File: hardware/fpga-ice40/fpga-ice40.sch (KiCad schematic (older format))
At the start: 88 parts, among them J1 MicroSD_Molex_1040310811, J2 Conn_01x03, J4 Conn_02x20_Odd_Even, J5 USB_B_Micro, J6 Conn_02x05_Odd_Even, J7 Conn_02x05_Odd_Even, Q1 2N7002H, U1 iCE40HX4K-TQ144, U2 IS42S16320F-6TL, U3 W25Q32JVSS, U4 W25Q32JVSS, U5 S25FL256SAGMFI01, U6 S25FL256SAGMFI01, U7 FT245RL, U8 AZ1117-1.2, U9 AZ1117-1.2, X1 ECS-2520MV-xxx-xx

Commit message: Clean up overhanging silkscreen on main 2x20 header
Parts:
- J4: footprint Connector_PinHeader_2.54mm:PinHeader_2x20_P2.54mm_Horizontal -> local_conn:PinHeader_2x20_P2.54mm_Horizontal
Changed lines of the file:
@@
 F 0 "J4" H 8950 15150 50  0000 C CNN
 F 1 "Conn_02x20_Odd_Even" H 8950 15125 50  0001 C CNN
-F 2 "Connector_PinHeader_2.54mm:PinHeader_2x20_P2.54mm_Horizontal" H 8900 14100 50  0001 C CNN
+F 2 "local_conn:PinHeader_2x20_P2.54mm_Horizontal" H 8900 14100 50  0001 C CNN
 F 3 "~" H 8900 14100 50  0001 C CNN
 	1    8900 14100

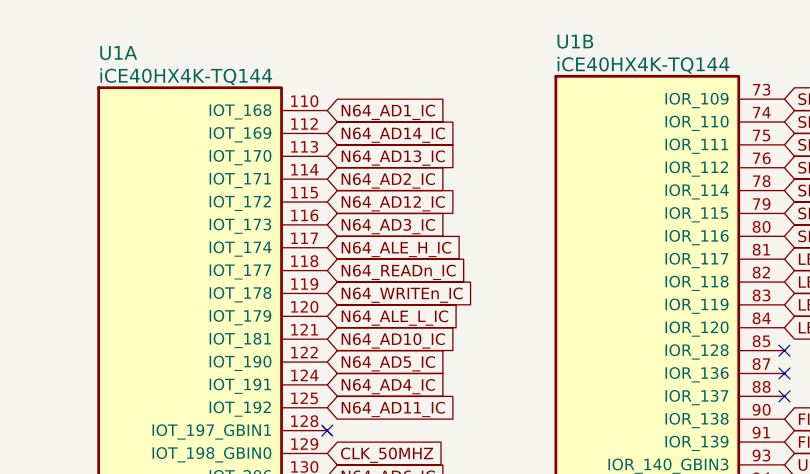
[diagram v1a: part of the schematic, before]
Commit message: N64 cart bus track glossing and front silkscreen cleanup
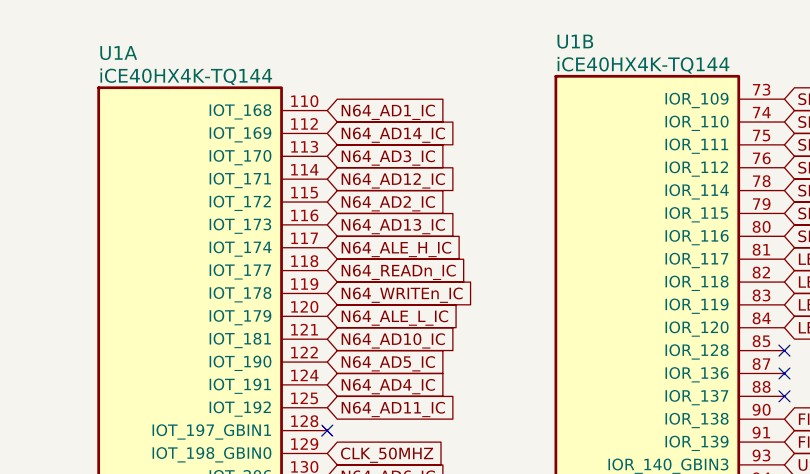
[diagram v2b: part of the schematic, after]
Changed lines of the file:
@@
 Text GLabel 2500 1600 2    50   Input ~ 0
 N64_AD1_IC
-Text GLabel 2500 1900 2    50   Input ~ 0
+Text GLabel 2500 2000 2    50   Input ~ 0
 N64_AD2_IC
-Text GLabel 2500 2100 2    50   Input ~ 0
+Text GLabel 2500 1800 2    50   Input ~ 0
 N64_AD3_IC
 Text GLabel 2500 2500 2    50   Input ~ 0
@@
 Text GLabel 2500 2300 2    50   Input ~ 0
 N64_READn_IC
-Text GLabel 2500 1800 2    50   Input ~ 0
+Text GLabel 2500 2100 2    50   Input ~ 0
 N64_AD13_IC
-Text GLabel 2500 2000 2    50   Input ~ 0
+Text GLabel 2500 1900 2    50   Input ~ 0
 N64_AD12_IC
 Text GLabel 2500 2900 2    50   Input ~ 0

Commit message: Use FTSH footprint with mating geometry and cleanup silkscreen
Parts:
- J6, J7: footprint ng_conn:Samtec_FTSH-105-XX-X-DV -> ng_conn:Samtec_FTSH-105-XX-X-DV-Mating
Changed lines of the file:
@@
 F 0 "J6" H 21700 7250 50  0000 C CNN
 F 1 "Conn_02x05_Odd_Even" H 21700 7276 50  0001 C CNN
-F 2 "ng_conn:Samtec_FTSH-105-XX-X-DV" H 21650 6950 50  0001 C CNN
+F 2 "ng_conn:Samtec_FTSH-105-XX-X-DV-Mating" H 21650 6950 50  0001 C CNN
 F 3 "~" H 21650 6950 50  0001 C CNN
 	1    21650 6950
@@
 F 0 "J7" H 21650 9350 50  0000 C CNN
 F 1 "Conn_02x05_Odd_Even" H 21650 9376 50  0001 C CNN
-F 2 "ng_conn:Samtec_FTSH-105-XX-X-DV" H 21600 9050 50  0001 C CNN
+F 2 "ng_conn:Samtec_FTSH-105-XX-X-DV-Mating" H 21600 9050 50  0001 C CNN
 F 3 "~" H 21600 9050 50  0001 C CNN
 	1    21600 9050

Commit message: Cleanup routing
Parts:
- X1: footprint Oscillator:Oscillator_SMD_ECS_2520MV-xxx-xx-4Pin_2.5x2.0mm -> ng_time:Oscillator_2.5x2.0
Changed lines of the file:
@@
 Text GLabel 21300 9150 0    50   Input ~ 0
 FLASH_MISO|IO1
-Text GLabel 21300 9250 0    50   Input ~ 0
-FLASH_IO2
-Text GLabel 21300 8950 0    50   Input ~ 0
-FLASH_IO3
 Wire Wire Line
 	12350 2450 12450 2450
@@
 Text GLabel 12950 13500 0    50   Input ~ 0
 N64_AD10
-Text GLabel 12950 14100 0    50   Input ~ 0
+Text GLabel 12950 14000 0    50   Input ~ 0
 N64_AD9
-Text GLabel 12950 14300 0    50   Input ~ 0
+Text GLabel 12950 14200 0    50   Input ~ 0
 N64_AD8
 $Comp
@@
 Text GLabel 12950 13600 0    50   Input ~ 0
 N64_AD5
-Text GLabel 12950 14000 0    50   Input ~ 0
+Text GLabel 12950 14100 0    50   Input ~ 0
 N64_AD6
-Text GLabel 12950 14200 0    50   Input ~ 0
+Text GLabel 12950 14300 0    50   Input ~ 0
 N64_AD7
 Text GLabel 11500 13400 2    50   Input ~ 0
@@
 Text GLabel 13350 13500 2    50   Input ~ 0
 N64_AD10_IC
-Text GLabel 13350 14100 2    50   Input ~ 0
+Text GLabel 13350 14000 2    50   Input ~ 0
 N64_AD9_IC
-Text GLabel 13350 14300 2    50   Input ~ 0
+Text GLabel 13350 14200 2    50   Input ~ 0
 N64_AD8_IC
 Text GLabel 13350 14800 2    50   Input ~ 0
@@
 Text GLabel 13350 13600 2    50   Input ~ 0
 N64_AD5_IC
-Text GLabel 13350 14000 2    50   Input ~ 0
+Text GLabel 13350 14100 2    50   Input ~ 0
 N64_AD6_IC
-Text GLabel 13350 14200 2    50   Input ~ 0
+Text GLabel 13350 14300 2    50   Input ~ 0
 N64_AD7_IC
 Text GLabel 4500 4350 2    50   Input ~ 0
@@
 Text GLabel 2500 2400 2    50   Input ~ 0
 N64_WRITEn_IC
+Text GLabel 2500 2100 2    50   Input ~ 0
+N64_READn_IC
 Text GLabel 2500 2300 2    50   Input ~ 0
-N64_READn_IC
-Text GLabel 2500 2100 2    50   Input ~ 0
 N64_AD13_IC
 Text GLabel 2500 1900 2    50   Input ~ 0
@@
 Text GLabel 2500 2600 2    50   Input ~ 0
 N64_AD10_IC
-Text GLabel 2500 3300 2    50   Input ~ 0
+Text GLabel 2500 3200 2    50   Input ~ 0
 N64_AD9_IC
-Text GLabel 2500 3500 2    50   Input ~ 0
+Text GLabel 2500 3400 2    50   Input ~ 0
 N64_AD8_IC
 Text GLabel 2500 3700 2    50   Input ~ 0
@@
 Text GLabel 2500 2700 2    50   Input ~ 0
 N64_AD5_IC
-Text GLabel 2500 3200 2    50   Input ~ 0
+Text GLabel 2500 3300 2    50   Input ~ 0
 N64_AD6_IC
-Text GLabel 2500 3400 2    50   Input ~ 0
+Text GLabel 2500 3500 2    50   Input ~ 0
 N64_AD7_IC
 Text GLabel 8500 2800 2    50   Input ~ 0
@@
 NoConn ~ 21900 9150
 Wire Wire Line
-	21300 8950 21400 8950
-Wire Wire Line
 	21400 9250 21300 9250
 Wire Wire Line
@@
 F 0 "X1" H 14900 3250 50  0000 L CNN
 F 1 "ECS-2520MV-xxx-xx" H 14850 2750 50  0000 L CNN
-F 2 "Oscillator:Oscillator_SMD_ECS_2520MV-xxx-xx-4Pin_2.5x2.0mm" H 15250 2650 50  0001 C CNN
+F 2 "ng_time:Oscillator_2.5x2.0" H 15250 2650 50  0001 C CNN
 F 3 "https://www.ecsxtal.com/store/pdf/ECS-2520MV.pdf" H 14625 3125 50  0001 C CNN
 	1    14800 3000
@@
 	1    0    0    -1
 $EndComp
+Text GLabel 21300 9250 0    50   Input ~ 0
+FLASH_IO2
+Wire Wire Line
+	21300 8950 21400 8950
+Text GLabel 21300 8950 0    50   Input ~ 0
+FLASH_IO3
 $EndSCHEMATC

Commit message: Divide 'fpga-ice40' schematic into multiple sheets
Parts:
- removed C1, C10, C11, C12, C13, C14, C15, C16, C17, C18, C19, C2, C20, C21, C22, C23, C24, C26, C28, C29, C3, C33, C4, C41, C43, C6, C7, C8, C9: 100n, Capacitor_SMD:C_0603_1608Metric, symbol Device:C
- removed C25, C30, C31, C5: 10u, Capacitor_SMD:C_0603_1608Metric, symbol Device:C
- removed C27, C34, C35, C36, C37, C38, C44: 10u, Capacitor_SMD:C_0805_2012Metric, symbol Device:C
- removed C32: 1u, Capacitor_SMD:C_0603_1608Metric, symbol Device:C
- removed C39, C40, C42: 10n, Capacitor_SMD:C_0603_1608Metric, symbol Device:C
- removed D1: ~~800mVf, Diode_SMD:D_SOD-123, symbol Device:D_Schottky
- removed D2, D3, D4, D5, D6: Blue, LED_SMD:LED_0603_1608Metric, symbol Device:LED
- removed FB1: 33R, 500mA, Inductor_SMD:L_0603_1608Metric, symbol Device:Ferrite_Bead
- removed J1: MicroSD_Molex_1040310811, ng_conn:MicroSD_Molex_1040310811, symbol ng_conn:MicroSD_Molex_1040310811
- removed J2: Conn_01x03, Connector_PinHeader_2.54mm:PinHeader_1x03_P2.54mm_Vertical, symbol Connector_Generic:Conn_01x03
- removed J4: Conn_02x20_Odd_Even, local_conn:PinHeader_2x20_P2.54mm_Horizontal, symbol Connector_Generic:Conn_02x20_Odd_Even
- removed J5: USB_B_Micro, Connector_USB:USB_Micro-B_Molex_47346-0001, symbol ng_conn:USB_B_Micro
- removed J6, J7: Conn_02x05_Odd_Even, ng_conn:Samtec_FTSH-105-XX-X-DV-Mating, symbol Connector_Generic:Conn_02x05_Odd_Even
- removed Q1: 2N7002H, Package_TO_SOT_SMD:SOT-23, symbol Transistor_FET:2N7002H
- removed R1, R2, R4, R8, R9: 10k, Resistor_SMD:R_0603_1608Metric, symbol Device:R
- removed R11, R12: 100R, Resistor_SMD:R_0603_1608Metric, symbol Device:R
- removed R3: 6k8, Resistor_SMD:R_0603_1608Metric, symbol Device:R
- removed R5: 470R, Resistor_SMD:R_0603_1608Metric, symbol Device:R
- removed R6: 100k, Resistor_SMD:R_0603_1608Metric, symbol Device:R
- removed R7: 330R, Resistor_SMD:R_Array_Convex_4x0603, symbol Device:R_Pack04_Split
- removed RN1, RN2, RN3: 10k, Resistor_SMD:R_Array_Convex_4x0603, symbol Device:R_Pack04
- removed RN4, RN5, RN6, RN7, RN8, RN9: 33R, Resistor_SMD:R_Array_Convex_4x0603, symbol Device:R_Pack04
- removed U1: iCE40HX4K-TQ144, Package_QFP:TQFP-144_20x20mm_P0.5mm, symbol ng_fpga_lattice_ice40:iCE40HX4K-TQ144
- removed U2: IS42S16320F-6TL, Package_SO:TSOP-II-54_22.2x10.16mm_P0.8mm, symbol ng_memory:IS42S16320F-6TL
- removed U3, U4: W25Q32JVSS, local_hacks:SOIC-8_5.275x5.275mm_P1.27mm__No_CrtYd, symbol ng_memory:W25Q32JVSS
- removed U5, U6: S25FL256SAGMFI01, Package_SO:SOIC-16W_7.5x10.3mm_P1.27mm, symbol ng_memory:S25FL256SAGMFI01
- removed U7: FT245RL, Package_SO:SSOP-28_5.3x10.2mm_P0.65mm, symbol ng_ftdi:FT245RL
- removed U8, U9: AZ1117-1.2, Package_TO_SOT_SMD:SOT-223-3_TabPin2, symbol Regulator_Linear:AZ1117-1.2
- removed X1: ECS-2520MV-xxx-xx, ng_time:Oscillator_2.5x2.0, symbol Oscillator:ECS-2520MV-xxx-xx
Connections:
- net labels removed: CLK_50MHZ, CONFIG_IO2, CONFIG_IO3, CONFIG_MISO|IO1, CONFIG_MOSI|IO0, CONFIG_SCK, CONFIG_SSn, DRAM_A0, DRAM_A1, DRAM_A10, DRAM_A11, DRAM_A12, DRAM_A2, DRAM_A3, DRAM_A4, DRAM_A5, DRAM_A6, DRAM_A7, DRAM_A8, DRAM_A9, DRAM_BA0, DRAM_BA1, DRAM_CASn, DRAM_CKE, DRAM_CLK, DRAM_CSn, DRAM_DQ0, DRAM_DQ1, DRAM_DQ10, DRAM_DQ11, DRAM_DQ12, DRAM_DQ13, DRAM_DQ14, DRAM_DQ15, DRAM_DQ2, DRAM_DQ3, DRAM_DQ4, DRAM_DQ5, DRAM_DQ6, DRAM_DQ7, DRAM_DQ8, DRAM_DQ9, DRAM_LDQM, DRAM_RASn, DRAM_UDQM, DRAM_WEn, FIFO_D0, FIFO_D1, FIFO_D2, FIFO_D3, FIFO_D4, FIFO_D5, FIFO_D6, FIFO_D7, FIFO_RDn, FIFO_RXFn, FIFO_TXEn, FIFO_WR, FLASH_IO2, FLASH_IO3, FLASH_MISO|IO1, FLASH_MOSI|IO0, FLASH_SCK, FLASH_SSn, FPGA_CDONE, FPGA_CRESETn, GND, LED_D0, LED_D1, LED_D2, LED_D3, N64_3V3, N64_AD0, N64_AD0_IC, N64_AD1, N64_AD10, N64_AD10_IC, N64_AD11, N64_AD11_IC, N64_AD12, N64_AD12_IC, N64_AD13, N64_AD13_IC, N64_AD14, N64_AD14_IC, N64_AD15, N64_AD15_IC, N64_AD1_IC, N64_AD2, N64_AD2_IC, N64_AD3, N64_AD3_IC, N64_AD4, N64_AD4_IC, N64_AD5, N64_AD5_IC, N64_AD6, N64_AD6_IC, N64_AD7, N64_AD7_IC, N64_AD8, N64_AD8_IC, N64_AD9, N64_AD9_IC, N64_ALE_H, N64_ALE_H_IC, N64_ALE_L, N64_ALE_L_IC, N64_COLD_RESETn, N64_COLD_RESETn_IC, N64_OS_EVENTn, N64_OS_EVENTn_IC, N64_READn, N64_READn_IC, N64_WRITEn, N64_WRITEn_IC, P1V2, P3V3, SD_CD, SD_CLK, SD_CMD, SD_DAT0, SD_DAT1, SD_DAT2, SD_DAT3, USB_3V3, USB_5V, USB_D+, USB_D-, USB_DETn, USB_PWRENn, USB_SHD, USB_VBUS, USB_VIO, VCC2V5, VCCGND0, VCCGND1, VCCPLL0, VCCPLL1
- wire segments 503 -> 0
- no-connect marks 29 -> 0
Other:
- note added: "FPGA"
- note added: "Interface"
- note added: "Memory"
- note added: "Misc"

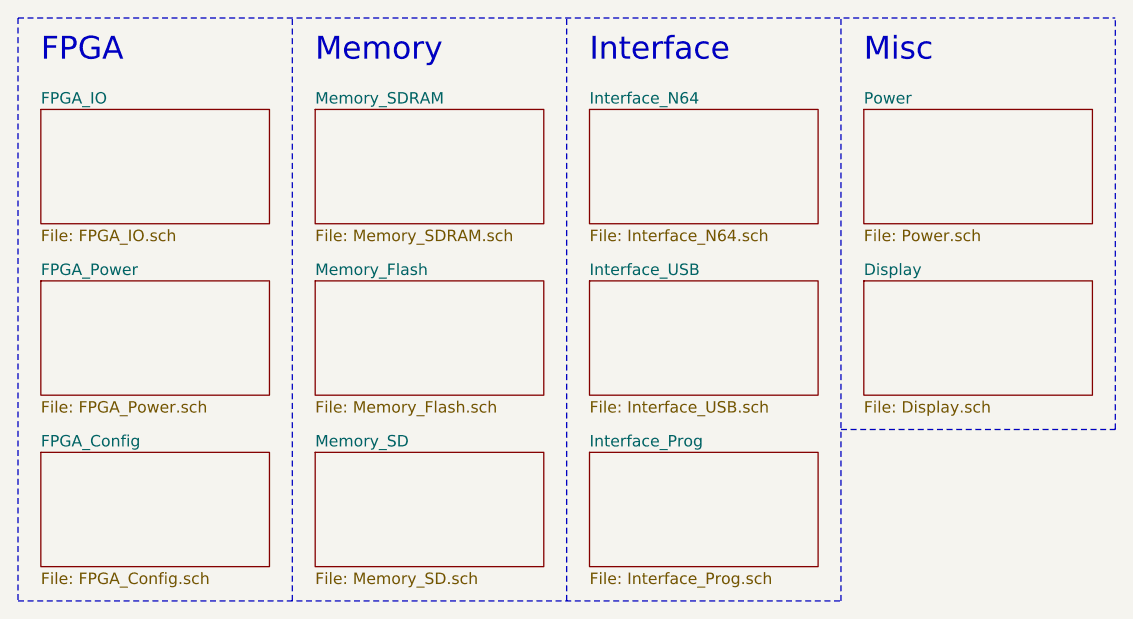
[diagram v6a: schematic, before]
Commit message: Add fiducial markers to FPGA
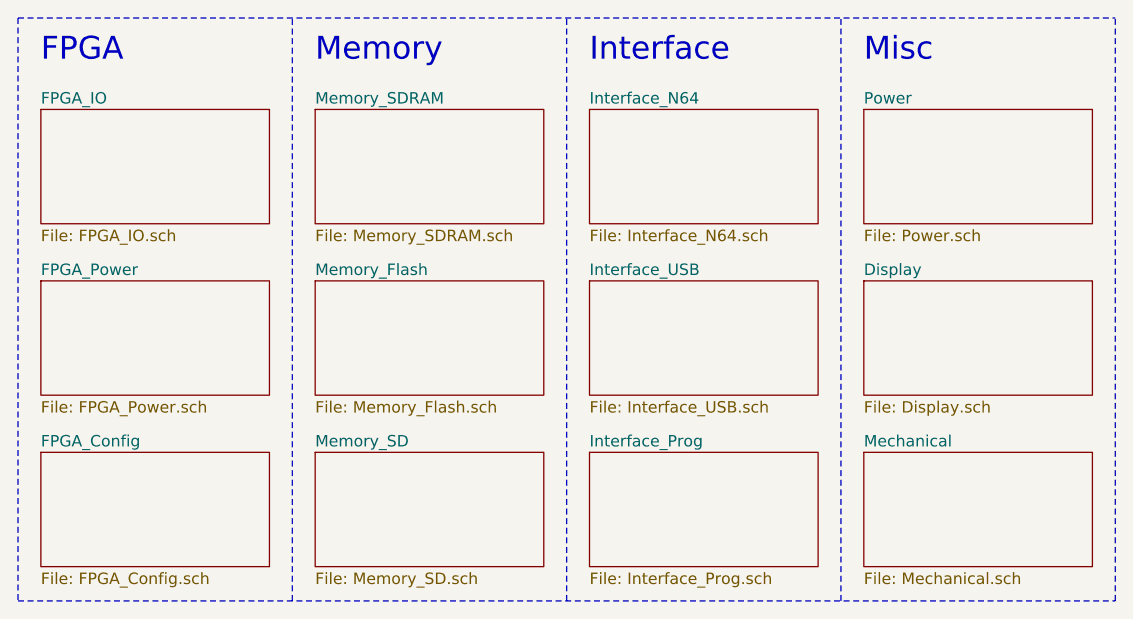
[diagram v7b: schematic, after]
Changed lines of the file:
@@
 $Descr USLetter 11000 8500
 encoding utf-8
-Sheet 1 12
+Sheet 1 13
 Title "Ferk-Cart iCE40 Devboard"
 Date "2020-06-29"
@@
 	6750 5500 6750 2950
 Wire Notes Line
-	6750 4750 7950 4750
-Wire Notes Line
-	7950 4750 7950 2950
-Wire Notes Line
-	3150 5500 6750 5500
+	7950 5500 7950 2950
 Text Notes 4450 3150 0    100  ~ 0
 Memory
@@
 F1 "Display.sch" 50
 $EndSheet
+Wire Notes Line
+	3150 5500 7950 5500
+$Sheet
+S 6850 4850 1000 500
+U 5F487C1E
+F0 "Mechanical" 50
+F1 "Mechanical.sch" 50
+$EndSheet
 $EndSCHEMATC
